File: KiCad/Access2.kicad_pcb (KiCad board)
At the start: 2 copper layers, 50 x 26.5 mm, 65 parts, among them J1 USB-C, J2 RFID, J3 INPUTS, J4 ExtTamper, J5 POWER, J6 DOOR, Q1 NX7002AK, SW1 Tamper, U1 ESP32-PICO-MINI-02, U2 FT231XQ, U3 G3VM-41GR8, U4 LMR16006+FB, U5 LMR16006+FB, U6 AA, U7 QR

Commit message: Tweak
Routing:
- net +12V: track 62.7 -> 62.5 mm, vias 1 -> 2
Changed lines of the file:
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@@
   (segment (start 128.620662 85.951956) (end 116.098352 85.951956) (width 0.25) (layer "B.Cu") (net 9))
   (segment (start 132.25 78) (end 131.098531 79.151469) (width 0.25) (layer "B.Cu") (net 9))
-  (segment (start 118.514852 83.746481) (end 118.514852 83.183896) (width 0.25) (layer "F.Cu") (net 10))
-  (segment (start 118.039296 84.300999) (end 118.136519 84.300999) (width 0.25) (layer "F.Cu") (net 10))
-  (segment (start 118.451458 83.809875) (end 118.514852 83.746481) (width 0.25) (layer "F.Cu") (net 10))
+  (segment (start 118.529927 82.779927) (end 118.529927 83.168821) (width 0.25) (layer "F.Cu") (net 10))
   (segment (start 131.4375 76.7) (end 128.849198 76.7) (width 0.25) (layer "F.Cu") (net 10))
-  (segment (start 118.451458 83.98606) (end 118.451458 83.809875) (width 0.25) (layer "F.Cu") (net 10))
-  (segment (start 116.9 84.95) (end 117.390295 84.95) (width 0.25) (layer "F.Cu") (net 10))
-  (segment (start 118.136519 84.300999) (end 118.451458 83.98606) (width 0.25) (layer "F.Cu") (net 10))
-  (segment (start 118.514852 83.183896) (end 118.529927 83.168821) (width 0.25) (layer "F.Cu") (net 10))
+  (segment (start 117.390295 84.95) (end 116.9 84.95) (width 0.25) (layer "F.Cu") (net 10))
   (segment (start 128.849198 76.7) (end 128.822959 76.726239) (width 0.25) (layer "F.Cu") (net 10))
-  (segment (start 118.529927 83.168821) (end 118.529927 82.779927) (width 0.25) (layer "F.Cu") (net 10))
-  (segment (start 117.390295 84.95) (end 118.039296 84.300999) (width 0.25) (layer "F.Cu") (net 10))
+  (segment (start 117.795148 84.545148) (end 117.390295 84.95) (width 0.25) (layer "F.Cu") (net 10))
+  (segment (start 117.795148 83.9036) (end 117.795148 84.545148) (width 0.25) (layer "F.Cu") (net 10))
+  (segment (start 118.529927 83.168821) (end 117.795148 83.9036) (width 0.25) (layer "F.Cu") (net 10))
   (via (at 128.822959 76.726239) (size 0.8) (drill 0.4) (layers "F.Cu" "B.Cu") (net 10))
   (via (at 118.529927 82.779927) (size 0.8) (drill 0.4) (layers "F.Cu" "B.Cu") (net 10))
@@
   (segment (start 131.727456 87.522544) (end 132.75 86.5) (width 0.25) (layer "B.Cu") (net 16))
   (segment (start 113.75 88) (end 114.44951 87.30049) (width 0.25) (layer "B.Cu") (net 16))
-  (segment (start 119.089363 83.984452) (end 119.025969 84.047846) (width 0.5) (layer "F.Cu") (net 17))
-  (segment (start 119.586988 82.924242) (end 119.089363 83.421867) (width 0.5) (layer "F.Cu") (net 17))
+  (segment (start 119.02548 84.97452) (end 119.02548 85.22452) (width 0.5) (layer "F.Cu") (net 17))
   (segment (start 142 76.75) (end 143.5125 76.75) (width 0.5) (layer "F.Cu") (net 17))
-  (segment (start 121.25 82) (end 120.308249 82.941751) (width 0.5) (layer "F.Cu") (net 17))
   (segment (start 143.5125 76.75) (end 144.7625 75.5) (width 0.5) (layer "F.Cu") (net 17))
-  (segment (start 119.02548 84.22452) (end 119.02548 85.22452) (width 0.5) (layer "F.Cu") (net 17))
-  (segment (start 118.538415 85.22452) (end 118.339395 85.0255) (width 0.5) (layer "F.Cu") (net 17))
+  (segment (start 119.025969 83.485261) (end 119.025969 84.224031) (width 0.5) (layer "F.Cu") (net 17))
+  (segment (start 118.339395 85.0255) (end 118.9745 85.0255) (width 0.5) (layer "F.Cu") (net 17))
+  (segment (start 120.325758 82.924242) (end 119.586988 82.924242) (width 0.5) (layer "F.Cu") (net 17))
+  (segment (start 119.586988 82.924242) (end 119.025969 83.485261) (width 0.5) (layer "F.Cu") (net 17))
+  (segment (start 118.9745 85.0255) (end 119.02548 84.97452) (width 0.5) (layer "F.Cu") (net 17))
+  (segment (start 119.025969 84.224031) (end 119.02548 84.22452) (width 0.5) (layer "F.Cu") (net 17))
   (segment (start 121.65 89.775) (end 119.95 91.475) (width 0.25) (layer "F.Cu") (net 17))
-  (segment (start 119.025969 84.224031) (end 119.02548 84.22452) (width 0.5) (layer "F.Cu") (net 17))
-  (segment (start 120.29074 82.924242) (end 119.586988 82.924242) (width 0.5) (layer "F.Cu") (net 17))
   (segment (start 121.65 82) (end 121.25 82) (width 0.5) (layer "F.Cu") (net 17))
   (segment (start 119.02548 90.55048) (end 119.95 91.475) (width 0.5) (layer "F.Cu") (net 17))
-  (segment (start 120.308249 82.941751) (end 120.29074 82.924242) (width 0.5) (layer "F.Cu") (net 17))
   (segment (start 121.55 80.75) (end 122.5 80.75) (width 0.25) (layer "F.Cu") (net 17))
   (segment (start 119.02548 85.22452) (end 119.02548 90.55048) (width 0.5) (layer "F.Cu") (net 17))
-  (segment (start 119.02548 85.22452) (end 118.538415 85.22452) (width 0.5) (layer "F.Cu") (net 17))
-  (segment (start 119.089363 83.421867) (end 119.089363 83.984452) (width 0.5) (layer "F.Cu") (net 17))
   (segment (start 121.65 89.75) (end 121.65 89.775) (width 0.25) (layer "F.Cu") (net 17))
-  (segment (start 119.025969 84.047846) (end 119.025969 84.224031) (width 0.5) (layer "F.Cu") (net 17))
+  (segment (start 119.02548 84.22452) (end 119.02548 84.97452) (width 0.5) (layer "F.Cu") (net 17))
+  (segment (start 121.25 82) (end 120.325758 82.924242) (width 0.5) (layer "F.Cu") (net 17))
   (via (at 118.339395 85.0255) (size 0.8) (drill 0.4) (layers "F.Cu" "B.Cu") (net 17))
+  (via (at 118.339395 85.0255) (size 0.8) (drill 0.4) (layers "F.Cu" "B.Cu") (net 17))
+  (segment (start 142 76.75) (end 138.562481 76.75) (width 0.5) (layer "B.Cu") (net 17))
+  (segment (start 124.5 79.25) (end 117.25 79.25) (width 0.5) (layer "B.Cu") (net 17))
+  (segment (start 125.5 74.75) (end 125.125 75.125) (width 0.5) (layer "B.Cu") (net 17))
+  (segment (start 144.5 75.08654) (end 142.83654 76.75) (width 0.5) (layer "B.Cu") (net 17))
+  (segment (start 115 81.5) (end 115 82.277518) (width 0.5) (layer "B.Cu") (net 17))
+  (segment (start 142.83654 76.75) (end 142 76.75) (width 0.5) (layer "B.Cu") (net 17))
+  (segment (start 117.747982 85.0255) (end 118.339395 85.0255) (width 0.5) (layer "B.Cu") (net 17))
+  (segment (start 136.562481 74.75) (end 125.5 74.75) (width 0.5) (layer "B.Cu") (net 17))
   (segment (start 138.562481 76.75) (end 136.562481 74.75) (width 0.5) (layer "B.Cu") (net 17))
-  (segment (start 124.5 79.25) (end 117.25 79.25) (width 0.5) (layer "B.Cu") (net 17))
-  (segment (start 117.897971 85.175489) (end 117.987971 85.175489) (width 0.5) (layer "B.Cu") (net 17))
-  (segment (start 117.987971 85.175489) (end 118.13796 85.0255) (width 0.5) (layer "B.Cu") (net 17))
+  (segment (start 115 82.277518) (end 117.747982 85.0255) (width 0.5) (layer "B.Cu") (net 17))
+  (segment (start 125.125 75.125) (end 125.125 78.625) (width 0.5) (layer "B.Cu") (net 17))
+  (segment (start 117.25 79.25) (end 115 81.5) (width 0.5) (layer "B.Cu") (net 17))
   (segment (start 125.125 78.625) (end 124.5 79.25) (width 0.5) (layer "B.Cu") (net 17))
-  (segment (start 144.5 75.08654) (end 142.83654 76.75) (width 0.5) (layer "B.Cu") (net 17))
-  (segment (start 118.13796 85.0255) (end 118.339395 85.0255) (width 0.5) (layer "B.Cu") (net 17))
-  (segment (start 142.83654 76.75) (end 142 76.75) (width 0.5) (layer "B.Cu") (net 17))
-  (segment (start 115 81.5) (end 115 82.277518) (width 0.5) (layer "B.Cu") (net 17))
-  (segment (start 125.5 74.75) (end 125.125 75.125) (width 0.5) (layer "B.Cu") (net 17))
-  (segment (start 115 82.277518) (end 117.897971 85.175489) (width 0.5) (layer "B.Cu") (net 17))
-  (segment (start 125.125 75.125) (end 125.125 78.625) (width 0.5) (layer "B.Cu") (net 17))
-  (segment (start 142 76.75) (end 138.562481 76.75) (width 0.5) (layer "B.Cu") (net 17))
-  (segment (start 117.25 79.25) (end 115 81.5) (width 0.5) (layer "B.Cu") (net 17))
-  (segment (start 136.562481 74.75) (end 125.5 74.75) (width 0.5) (layer "B.Cu") (net 17))
   (segment (start 144.5 72.65) (end 144.5 75.08654) (width 0.5) (layer "B.Cu") (net 17))
   (segment (start 139.80049 82.186194) (end 139.80049 80.97549) (width 0.25) (layer "F.Cu") (net 18))
@@
   (segment (start 128.050099 76.474501) (end 127.199901 76.474501) (width 0.25) (layer "F.Cu") (net 24))
   (segment (start 127.199901 76.474501) (end 126.487701 75.762299) (width 0.25) (layer "F.Cu") (net 24))
-  (segment (start 119.60048 89.10048) (end 119.60048 84.285816) (width 0.25) (layer "F.Cu") (net 24))
+  (segment (start 119.60048 89.10048) (end 119.95 89.45) (width 0.25) (layer "F.Cu") (net 24))
   (segment (start 121.55 88.5) (end 121.362507 88.5) (width 0.25) (layer "F.Cu") (net 24))
+  (segment (start 119.95 89.45) (end 119.95 89.825) (width 0.25) (layer "F.Cu") (net 24))
+  (segment (start 119.60048 84.112127) (end 119.60048 89.10048) (width 0.25) (layer "F.Cu") (net 24))
   (segment (start 120.037507 89.825) (end 119.95 89.825) (width 0.25) (layer "F.Cu") (net 24))
-  (segment (start 119.692713 84.019894) (end 119.938864 83.773743) (width 0.25) (layer "F.Cu") (net 24))
-  (segment (start 119.692713 84.193583) (end 119.692713 84.019894) (width 0.25) (layer "F.Cu") (net 24))
-  (segment (start 119.95 89.45) (end 119.60048 89.10048) (width 0.25) (layer "F.Cu") (net 24))
   (segment (start 128.474501 75.800099) (end 128.474501 76.050099) (width 0.25) (layer "F.Cu") (net 24))
   (segment (start 128.5246 75.75) (end 128.474501 75.800099) (width 0.25) (layer "F.Cu") (net 24))
   (segment (start 129.5625 75.75) (end 128.5246 75.75) (width 0.25) (layer "F.Cu") (net 24))
+  (segment (start 119.938864 83.773743) (end 119.60048 84.112127) (width 0.25) (layer "F.Cu") (net 24))
   (segment (start 121.362507 88.5) (end 120.037507 89.825) (width 0.25) (layer "F.Cu") (net 24))
   (segment (start 128.474501 76.050099) (end 128.050099 76.474501) (width 0.25) (layer "F.Cu") (net 24))
-  (segment (start 119.60048 84.285816) (end 119.692713 84.193583) (width 0.25) (layer "F.Cu") (net 24))
-  (segment (start 119.95 89.825) (end 119.95 89.45) (width 0.25) (layer "F.Cu") (net 24))
   (via (at 126.487701 75.762299) (size 0.8) (drill 0.4) (layers "F.Cu" "B.Cu") (net 24))
   (via (at 119.938864 83.773743) (size 0.8) (drill 0.4) (layers "F.Cu" "B.Cu") (net 24))

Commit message: Curvy tracks
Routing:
- net Net-(Q1-Pad3): track 30.2 -> 37.3 mm
- net SHDN: track 21.3 -> 26.1 mm
- net Net-(R22-Pad2): track 17.9 -> 21.4 mm
- net +12V: track 62.5 -> 59.5 mm, vias 2 -> 1
- net GND: track 67.4 -> 65.3 mm, vias 10 -> 11
- net G: track 34.7 -> 35.8 mm
- net O: track 31.2 -> 32.1 mm
- net IN1: track 17.1 -> 16.2 mm
- net Net-(J1-PadA7): track 16.6 -> 15.7 mm
- net B: track 33.7 -> 34.5 mm
- net IN4: track 16.0 -> 15.2 mm
- net IN6: track 17.2 -> 16.6 mm
- net Net-(J1-PadA6): track 11.8 -> 11.2 mm
- net TAMPER: track 33.6 -> 34.1 mm
- net Net-(R2-Pad2): track 19.6 -> 19.0 mm

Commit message: Started Keypad2 - may scrap it though.
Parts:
- R17: value 732R -> 680R
- R19: value 324R -> 220R
- U2: footprint RevK:QFN-20-1EP_4x4mm_P0.5mm_EP2.5x2.5mm -> Package_DFN_QFN:QFN-20-1EP_4x4mm_P0.5mm_EP2.5x2.5mm

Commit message: Cleanup
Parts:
- moved AJK1 0.38 mm to (109.7, 85.5)
- moved U3 0.25 mm to (136.5, 76.2)
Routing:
- net +3V3: track 133.7 -> 133.2 mm
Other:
- board text added: "Solar System Access Control"

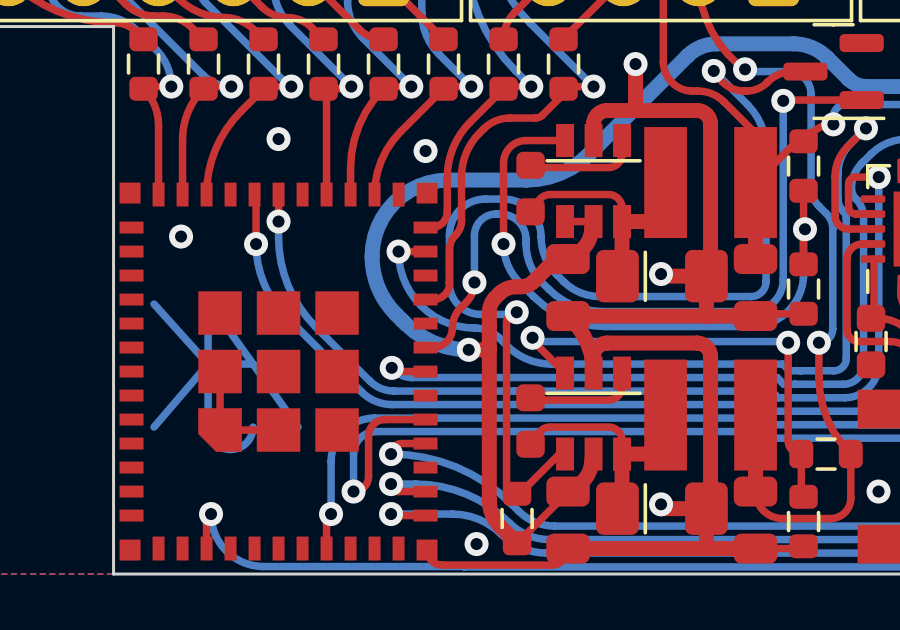
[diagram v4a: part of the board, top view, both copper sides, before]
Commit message: Tweaked some GPIO, and added to documentation
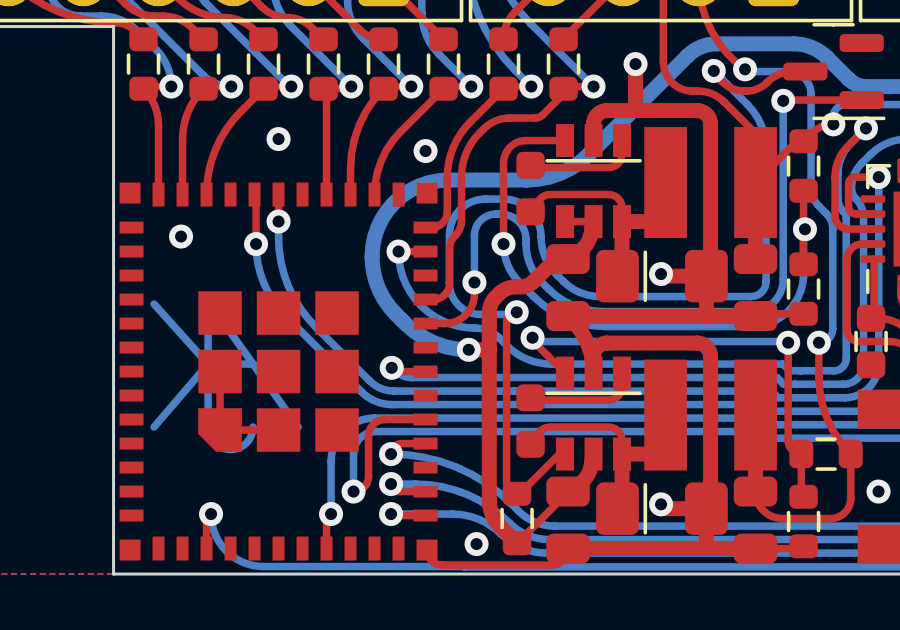
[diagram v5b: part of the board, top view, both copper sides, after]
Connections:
- U1 pad 19: SHDN -> unconnected-(U1-Pad19)
- U1 pad 20: unconnected-(U1-Pad20) -> SHDN
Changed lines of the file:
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@@
   (net 60 "unconnected-(U1-Pad29)")
   (net 61 "unconnected-(U1-Pad25)")
-  (net 62 "unconnected-(U1-Pad20)")
+  (net 62 "unconnected-(U1-Pad19)")
   (net 63 "unconnected-(U1-Pad17)")
   (net 64 "unconnected-(U2-Pad16)")
@@
       (net 9 "OUT1") (pinfunction "IO14") (pintype "bidirectional"))
     (pad "19" smd rect (at 0.8 4.9 90) (size 0.4 0.8) (layers "F.Cu" "F.Paste" "F.Mask")
-      (net 10 "SHDN") (pinfunction "IO12") (pintype "bidirectional"))
+      (net 62 "unconnected-(U1-Pad19)") (pinfunction "IO12") (pintype "bidirectional+no_connect"))
     (pad "20" smd rect (at 1.6 4.9 90) (size 0.4 0.8) (layers "F.Cu" "F.Paste" "F.Mask")
-      (net 62 "unconnected-(U1-Pad20)") (pinfunction "IO13") (pintype "bidirectional+no_connect"))
+      (net 10 "SHDN") (pinfunction "IO13") (pintype "bidirectional"))
     (pad "21" smd rect (at 2.4 4.9 90) (size 0.4 0.8) (layers "F.Cu" "F.Paste" "F.Mask")
       (net 5 "RFRX") (pinfunction "IO15") (pintype "bidirectional"))
@@
   (arc (start 131.098531 79.634322) (mid 131.187265 79.188224) (end 131.43996 78.810041) (width 0.25) (layer "B.Cu") (net 9))
   (arc (start 131.25 80) (mid 131.137896 79.832226) (end 131.098531 79.634322) (width 0.25) (layer "B.Cu") (net 9))
-  (segment (start 116.9 84.95) (end 117.140296 84.95) (width 0.25) (layer "F.Cu") (net 10))
+  (segment (start 118.529927 82.779927) (end 118.529927 83.170073) (width 0.25) (layer "F.Cu") (net 10))
   (segment (start 131.4375 76.7) (end 128.849198 76.7) (width 0.25) (layer "F.Cu") (net 10))
+  (segment (start 117.55 84.15) (end 116.9 84.15) (width 0.25) (layer "F.Cu") (net 10))
   (segment (start 128.849198 76.7) (end 128.822959 76.726239) (width 0.25) (layer "F.Cu") (net 10))
-  (segment (start 118.149374 83.549374) (end 118.072014 83.626734) (width 0.25) (layer "F.Cu") (net 10))
-  (segment (start 118.254937 83.44381) (end 118.149374 83.549374) (width 0.25) (layer "F.Cu") (net 10))
   (via (at 128.822959 76.726239) (size 0.8) (drill 0.4) (layers "F.Cu" "B.Cu") (net 10))
   (via (at 118.529927 82.779927) (size 0.8) (drill 0.4) (layers "F.Cu" "B.Cu") (net 10))
-  (arc (start 118.529927 82.779927) (mid 118.45846 83.139218) (end 118.254937 83.44381) (width 0.25) (layer "F.Cu") (net 10))
-  (arc (start 118.072014 83.626734) (mid 117.867103 83.933405) (end 117.795148 84.295148) (width 0.25) (layer "F.Cu") (net 10))
-  (arc (start 117.140296 84.95) (mid 117.603346 84.758198) (end 117.795148 84.295148) (width 0.25) (layer "F.Cu") (net 10))
+  (arc (start 118.529927 83.170073) (mid 118.242913 83.862986) (end 117.55 84.15) (width 0.25) (layer "F.Cu") (net 10))
   (segment (start 120.25 81.5) (end 120.25 81.353553) (width 0.25) (layer "B.Cu") (net 10))
   (segment (start 118.529927 82.779927) (end 118.529927 81.220073) (width 0.25) (layer "B.Cu") (net 10))

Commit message: Tidy
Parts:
- U2: footprint Package_DFN_QFN:QFN-20-1EP_4x4mm_P0.5mm_EP2.5x2.5mm -> RevK:QFN-20-1EP_4x4mm_P0.5mm_EP2.5x2.5mm

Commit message: Tidy
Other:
- board text removed: "www.me.uk"
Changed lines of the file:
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@@
       (effects (font (size 1 1) (thickness 0.15)) (justify mirror))
     )
+    (fp_text user "www.me.uk" (at -0.58 -3.75 unlocked) (layer "B.SilkS")
+      (effects (font (size 0.65 0.65) (thickness 0.1)) (justify mirror))
+    )
+    (fp_line (start -0.85 -1.95) (end -0.75 -1.95) (layer "B.Cu") (width 0.08))
+    (fp_line (start 1.8 2) (end 0 0) (layer "B.Cu") (width 0.25))
+    (fp_line (start 0 0) (end 1.8 -2.1) (layer "B.Cu") (width 0.25))
+    (fp_line (start -0.75 -2.11) (end -0.65 -2.25) (layer "B.Cu") (width 0.08))
+    (fp_line (start -0.85 -2.11) (end -0.75 -2.11) (layer "B.Cu") (width 0.08))
+    (fp_line (start 0 0) (end -1.5 0) (layer "B.Cu") (width 0.25))
+    (fp_line (start 0 2.1) (end -3 -2.1) (layer "B.Cu") (width 0.25))
+    (fp_line (start -0.85 -1.95) (end -0.85 -2.25) (layer "B.Cu") (width 0.08))
     (fp_line (start 0 2.1) (end 0 -2.1) (layer "B.Cu") (width 0.25))
-    (fp_line (start -0.85 -1.95) (end -0.75 -1.95) (layer "B.Cu") (width 0.08))
-    (fp_line (start -0.75 -2.11) (end -0.65 -2.25) (layer "B.Cu") (width 0.08))
-    (fp_line (start -0.85 -1.95) (end -0.85 -2.25) (layer "B.Cu") (width 0.08))
-    (fp_line (start 0 0) (end -1.5 0) (layer "B.Cu") (width 0.25))
-    (fp_line (start 0 0) (end 1.8 -2.1) (layer "B.Cu") (width 0.25))
-    (fp_line (start -0.85 -2.11) (end -0.75 -2.11) (layer "B.Cu") (width 0.08))
-    (fp_line (start 1.8 2) (end 0 0) (layer "B.Cu") (width 0.25))
-    (fp_line (start 0 2.1) (end -3 -2.1) (layer "B.Cu") (width 0.25))
     (fp_arc (start -0.75 -2.11) (mid -0.67 -2.03) (end -0.75 -1.95) (layer "B.Cu") (width 0.08))
     (fp_arc (start -1.5 -2.1) (mid -0.75 -2.85) (end 0 -2.1) (layer "B.Cu") (width 0.25))
     (fp_circle (center -0.77 -2.11) (end -0.47 -2.11) (layer "B.Cu") (width 0.08) (fill none))
+    (fp_line (start 1.8 2) (end 0 0) (layer "B.Mask") (width 0.45))
     (fp_line (start 0 0) (end -1.5 0) (layer "B.Mask") (width 0.45))
+    (fp_line (start 0 2.1) (end 0 -2.1) (layer "B.Mask") (width 0.45))
     (fp_line (start 0 2.1) (end -3 -2.1) (layer "B.Mask") (width 0.45))
-    (fp_line (start 1.8 2) (end 0 0) (layer "B.Mask") (width 0.45))
     (fp_line (start 0 0) (end 1.8 -2.1) (layer "B.Mask") (width 0.45))
-    (fp_line (start 0 2.1) (end 0 -2.1) (layer "B.Mask") (width 0.45))
     (fp_arc (start -1.5 -2.1) (mid -0.75 -2.85) (end 0 -2.1) (layer "B.Mask") (width 0.45))
   )
@@
     (effects (font (size 0.75 0.75) (thickness 0.1)) (justify left mirror))
   )
-  (gr_text "www.me.uk" (at 110.1 89.25) (layer "B.SilkS")
-    (effects (font (size 0.75 0.75) (thickness 0.1)) (justify mirror))
-  )
   (gr_text "16" (at 123.5 58.25) (layer "B.Fab")

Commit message: Clean up
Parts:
- moved JP1 1.18 mm to (142.7, 75.8), turned to -90 degrees
- moved R3 0.45 mm to (145.8, 77.7)
- moved D8 0.15 mm to (146.4, 75.5)
- moved R4 0.10 mm to (141.8, 85.1)
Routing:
- net Net-(J1-PadA7): track 15.7 -> 10.2 mm, vias 2 -> 0
- net Net-(J1-PadA6): track 11.2 -> 6.80 mm, vias 2 -> 0
- net VBUS: track 23.1 -> 20.7 mm, vias 0 -> 2
- net Net-(R2-Pad2): track 19.0 -> 17.9 mm
